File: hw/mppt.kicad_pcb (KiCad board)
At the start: 4 copper layers, 100 x 55 mm, 90 parts, among them J201 1935776, J202 BNC, J301 1935776, J302 1935776, J401 BNC, Q301 SW_L, Q302 SW_H, SW201 SW_Push, U201 MCU_Nucleo_L432KC, U401 OPA990, U402 INA210, U403 OPA990, U404 INA210, U501 LMG1210RVRT

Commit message: fixes for v0.1.1rc
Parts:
- removed C3042, C3052: 15uF, Capacitor_THT:C_Radial_D8.0mm_H11.5mm_P3.50mm
- C303: value 1uF -> 2.2uF
- moved REF** 1.25 mm to (128.2, 97.0)
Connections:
- U201 pad 5: /controller/Error -> unconnected-(U201-D2-Pad5)
- U201 pad 6: unconnected-(U201-D3-Pad6) -> /controller/Error
- U401 pad 1: /controller/ARR_V -> Net-(U401-IN+)
- U401 pad 3: Net-(U401-IN+) -> /controller/ARR_V
- U403 pad 1: /controller/BATT_V -> Net-(U403-IN+)
- U403 pad 3: Net-(U403-IN+) -> /controller/BATT_V
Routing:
- net /controller/Error: track 37.9 -> 40.4 mm
- net Net-(U403-IN+): track 6.05 -> 5.55 mm, vias 3 -> 2
- net GND: vias 524 -> 522
- net /V_ARR+: vias 168 -> 154
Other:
- board text added: "Sunscatter MPPT LHR Solar 2023 Jacob Pustilnik Matthew Yu v0.1.1"
- board text removed: "Jacob Pustilnik Matthew Yu ECE394J Sp2023"

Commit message: v0.2.0
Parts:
- removed D301: Schottky, TestPoint:TestPoint_2Pads_Pitch2.54mm_Drill0.8mm
- removed D302: D_TVS, Diode_SMD:D_SMC
- removed G***: LOGO, graphics:Texas Engineering
- removed HS301: Heatsink_Pad, mppt:WayinTop_HS
- removed J202, J401: BNC, mppt:CONBNC002
- removed R301: R, TestPoint:TestPoint_2Pads_Pitch2.54mm_Drill0.8mm
- removed the REF** at (128.2, 97.0)
- removed SW201: SW_Push, mppt:TS046643BK100SMT
- removed TJ104, TJ105: Thermal Jumper, Resistor_SMD:R_0805_2012Metric
- removed TJ106, TJ107: Thermal Jumper, mppt:1225_SMD
- removed TP205: GND MCU TP, TestPoint:TestPoint_Keystone_5000-5004_Miniature
- removed TP302: TestPoint_2Pole, mppt:SignalTP
- removed U401, U403: OPA990, mppt:SOT65P210X110-5N
- removed U402, U404: INA210, Package_TO_SOT_SMD:SOT-363_SC-70-6_Handsoldering
- removed U501: LMG1210RVRT, mppt:IC_LMG1210RVRT
- added C601: 10uF, Capacitor_SMD:C_0402_1005Metric, B.Cu at (125.5, 54.8)
- added C602: 100nF, Capacitor_SMD:C_0402_1005Metric, B.Cu at (126.9, 54.8)
- added C603: 100nF, Capacitor_SMD:C_0402_1005Metric, B.Cu at (125.5, 52.5)
- added C604: 10nF, Capacitor_SMD:C_0402_1005Metric, B.Cu at (126.9, 52.5)
- added C605: 220nF, Capacitor_SMD:C_0402_1005Metric, B.Cu at (117.5, 54.9)
- added C606: 10uF, Capacitor_SMD:C_0402_1005Metric, B.Cu at (113.6, 55.0)
- added C607: 10nF, Capacitor_SMD:C_0402_1005Metric, B.Cu at (116.2, 52.0)
- added C608: 100nF, Capacitor_SMD:C_0402_1005Metric, B.Cu at (114.8, 52.0)
- added D204: BLUE, LED_SMD:LED_0603_1608Metric, F.Cu at (184.0, 57.2)
- added D205: BLUE, LED_SMD:LED_0603_1608Metric, F.Cu at (184.0, 59.8)
- added D601: CDSOT23-T24CAN, footprints:bourns_CDSOT23_T24CAN, B.Cu at (122.6, 48.7)
- added F301: Fuse_Small, footprints:littelfuse_05200101Z, F.Cu at (90.3, 72.5)
- added F302: Fuse_Small, footprints:littelfuse_05200101Z, F.Cu at (175.6, 72.4)
- added IC401: INA210CQDCKRQ1, footprints:ti_INA210CQDCKRQ1, B.Cu at (102.5, 66.2)
- added IC402: OPA990IDCKR, footprints:ti_OPA990IDCKR, B.Cu at (118.7, 66.0)
- added IC403: OPA990IDCKR, footprints:ti_OPA990IDCKR, B.Cu at (178.3, 66.0)
- added IC404: INA210CQDCKRQ1, footprints:ti_INA210CQDCKRQ1, B.Cu at (187.7, 66.1)
- added IC501: LMG1210RVRT, footprints:ti_LMG1210RVRT, F.Cu at (166.6, 75.2)
- added IC601: ADM3055EBRIZ, footprints:analog_ADM3055EBRIZ, F.Cu at (124.1, 51.0)
- added J601: 43650-0427, footprints:molex_microfit_43650_0427, F.Cu at (97.7, 55.5)
- added J602: 43650-0427, footprints:molex_microfit_43650_0427, F.Cu at (108.3, 55.5)
- added JP601: Termination Resistors, Connector_PinHeader_2.54mm:PinHeader_1x02_P2.54mm_Vertical, F.Cu at (115.5, 43.7)
- added L601: 1.8k, Inductor_SMD:L_0402_1005Metric, B.Cu at (115.5, 55.6)
- added L602: 1.8k, Inductor_SMD:L_0402_1005Metric, B.Cu at (115.5, 54.2)
- added R203: 100, Resistor_SMD:R_0402_1005Metric, B.Cu at (168.6, 46.4)
- added R204: 100, Resistor_SMD:R_0402_1005Metric, B.Cu at (158.4, 46.4)
- added R205: 100, Resistor_SMD:R_0402_1005Metric, B.Cu at (138.1, 46.4)
- added R601: 0, Resistor_SMD:R_0402_1005Metric, B.Cu at (117.5, 46.0)
- added R602: 60.4, Resistor_SMD:R_0402_1005Metric, B.Cu at (115.5, 49.4)
- added R603: 60.4, Resistor_SMD:R_0402_1005Metric, B.Cu at (113.8, 49.5)
- added REF**: ESD-Logo_6.6x6mm_SilkScreen, Symbol:ESD-Logo_6.6x6mm_SilkScreen, B.Cu at (131.1, 91.0)
- added S201: TS-1187A-B-A-B, footprints:xkb_TS_1187A_B_A_B, F.Cu at (184.0, 45.0)
- added TP411: BATTV_TP, TestPoint:TestPoint_Pad_1.0x1.0mm, F.Cu at (161.9, 63.9)
- added TP412: BATTI_TP, TestPoint:TestPoint_Pad_1.0x1.0mm, F.Cu at (169.0, 63.9)
- added TP504: PWMEN_TP, TestPoint:TestPoint_Pad_1.0x1.0mm, B.Cu at (166.3, 70.7)
- added TP505: PWM_TP, TestPoint:TestPoint_Pad_1.0x1.0mm, B.Cu at (164.3, 70.7)
- added TP601: CAN RX TP, TestPoint:TestPoint_Pad_1.0x1.0mm, B.Cu at (128.9, 51.7)
- added TP602: CAN TX TP, TestPoint:TestPoint_Pad_1.0x1.0mm, B.Cu at (128.9, 49.1)
- added TP603: CAN L TP, TestPoint:TestPoint_Pad_1.0x1.0mm, B.Cu at (119.3, 47.7)
- added TP604: CAN H TP, TestPoint:TestPoint_Pad_1.0x1.0mm, B.Cu at (119.3, 49.3)
- added kibuzzard-64BB9525: G***, kibuzzard-64BB9525, F.Cu at (189.4, 52.3)
- added kibuzzard-64BB9530: G***, kibuzzard-64BB9530, F.Cu at (189.4, 49.8)
- added kibuzzard-64BB9539: G***, kibuzzard-64BB9539, F.Cu at (189.4, 54.8)
- added kibuzzard-64BB9548: G***, kibuzzard-64BB9548, F.Cu at (189.4, 59.9)
- added kibuzzard-64BB954F: G***, kibuzzard-64BB954F, F.Cu at (189.4, 57.2)
- added kibuzzard-64BB9585: G***, kibuzzard-64BB9585, F.Cu at (189.4, 45.0)
- added kibuzzard-64BB95E9: G***, kibuzzard-64BB95E9, F.Cu at (204.2, 57.0)
- added kibuzzard-64BB964A: G***, kibuzzard-64BB964A, F.Cu at (201.1, 53.0)
- added kibuzzard-64BB966B: G***, kibuzzard-64BB966B, F.Cu at (201.1, 56.0)
- added kibuzzard-64BB968B: G***, kibuzzard-64BB968B, F.Cu at (175.3, 51.0)
- added kibuzzard-64BB971E: G***, kibuzzard-64BB971E, F.Cu at (90.8, 58.8)
- added kibuzzard-64BB973A: G***, kibuzzard-64BB973A, F.Cu at (103.2, 46.5)
- added kibuzzard-64BB974F: G***, kibuzzard-64BB974F, F.Cu at (103.2, 49.5)
- added kibuzzard-64BB975A: G***, kibuzzard-64BB975A, F.Cu at (103.2, 55.5)
- added kibuzzard-64BB9776: G***, kibuzzard-64BB9776, F.Cu at (103.2, 52.5)
- added kibuzzard-64BB97BE: G***, kibuzzard-64BB97BE, F.Cu at (89.2, 90.8)
- added kibuzzard-64BB97CA: G***, kibuzzard-64BB97CA, F.Cu at (199.6, 90.8)
- added kibuzzard-64BB97F0: G***, kibuzzard-64BB97F0, B.Cu at (106.0, 98.3)
- added kibuzzard-64BB97F0: G***, kibuzzard-64BB97F0, B.Cu at (191.3, 98.2)
- added kibuzzard-64BB97FE: G***, kibuzzard-64BB97FE, B.Cu at (183.9, 98.1)
- added kibuzzard-64BB97FE: G***, kibuzzard-64BB97FE, B.Cu at (98.7, 98.3)
- added kibuzzard-64BB9873: G***, kibuzzard-64BB9873, F.Cu at (88.7, 87.8)
- added kibuzzard-64BB9873: G***, kibuzzard-64BB9873, F.Cu at (201.3, 87.8)
- added kibuzzard-64BB98F2: G***, kibuzzard-64BB98F2, F.Cu at (88.3, 81.6)
- added kibuzzard-64BB98F8: G***, kibuzzard-64BB98F8, F.Cu at (88.3, 84.7)
- added kibuzzard-64BB9946: G***, kibuzzard-64BB9946, F.Cu at (201.9, 84.7)
- added kibuzzard-64BB994C: G***, kibuzzard-64BB994C, F.Cu at (202.0, 81.5)
- added kibuzzard-64BBA694: G***, kibuzzard-64BBA694, F.Cu at (129.8, 63.8)
- added kibuzzard-64BBA6A3: G***, kibuzzard-64BBA6A3, F.Cu at (136.4, 63.8)
- added kibuzzard-64BBA6B0: G***, kibuzzard-64BBA6B0, F.Cu at (162.1, 66.2)
- added kibuzzard-64BBA6B0: G***, kibuzzard-64BBA6B0, F.Cu at (132.9, 66.0)
- added kibuzzard-64BBA752: G***, kibuzzard-64BBA752, F.Cu at (158.4, 63.9)
- added kibuzzard-64BBA758: G***, kibuzzard-64BBA758, F.Cu at (165.6, 63.9)
- added kibuzzard-64BBA88C: G***, kibuzzard-64BBA88C, B.Cu at (160.9, 54.1)
- added kibuzzard-64BBA896: G***, kibuzzard-64BBA896, B.Cu at (165.7, 54.0)
- added kibuzzard-64BBA8A0: G***, kibuzzard-64BBA8A0, B.Cu at (168.9, 54.0)
- added kibuzzard-64BBA8B2: G***, kibuzzard-64BBA8B2, B.Cu at (138.0, 56.0)
- added kibuzzard-64BBA8C3: G***, kibuzzard-64BBA8C3, B.Cu at (163.9, 68.8)
- added kibuzzard-64BBA8E6: G***, kibuzzard-64BBA8E6, B.Cu at (166.3, 68.8)
- added kibuzzard-64BBA9B6: G***, kibuzzard-64BBA9B6, F.Cu at (142.2, 67.5)
- added kibuzzard-64BBA9C0: G***, kibuzzard-64BBA9C0, F.Cu at (147.3, 67.4)
- added kibuzzard-64BBA9D4: G***, kibuzzard-64BBA9D4, F.Cu at (152.3, 67.4)
- added kibuzzard-64BBAA49: G***, kibuzzard-64BBAA49, F.Cu at (155.2, 78.3)
- added kibuzzard-64BBAA54: G***, kibuzzard-64BBAA54, F.Cu at (155.2, 73.2)
- added kibuzzard-64BC07CB: G***, kibuzzard-64BC07CB, B.Cu at (131.0, 49.1)
- added kibuzzard-64BC07D4: G***, kibuzzard-64BC07D4, B.Cu at (131.0, 51.7)
- added kibuzzard-64BC07E0: G***, kibuzzard-64BC07E0, B.Cu at (117.5, 47.7)
- added kibuzzard-64BC07EC: G***, kibuzzard-64BC07EC, B.Cu at (117.5, 49.3)
- C301: value 15uF -> 2.2uF; footprint Capacitor_THT:C_Radial_D8.0mm_H11.5mm_P3.50mm -> Capacitor_SMD:C_2220_5650Metric; moved to B.Cu
- C302: value CP -> 15uF; footprint TestPoint:TestPoint_2Pads_Pitch2.54mm_Drill0.8mm -> Capacitor_THT:C_Radial_D8.0mm_H11.5mm_P3.50mm
- C503: value 1uF -> 10uF; footprint Capacitor_SMD:C_0402_1005Metric -> Capacitor_SMD:C_0603_1608Metric
- C505: value 10uF -> 1uF; footprint Capacitor_SMD:C_0603_1608Metric -> Capacitor_SMD:C_0402_1005Metric
- D201: value RED -> YELLOW; footprint LED_SMD:LED_0402_1005Metric -> LED_SMD:LED_0603_1608Metric
- D202: value YELLOW -> GREEN; footprint LED_SMD:LED_0402_1005Metric -> LED_SMD:LED_0603_1608Metric
- D203: value BLUE -> GREEN; footprint LED_SMD:LED_0402_1005Metric -> LED_SMD:LED_0603_1608Metric
- D402, D403: value 3.3V Zener -> 3V3
- D501: value 0.62V Schottky -> 0.62V; footprint mppt:SODFL5226X110N -> footprints:stm_STPS1170AF
- H101, H102, H103, H104: footprint MountingHole:MountingHole_3.5mm -> MountingHole:MountingHole_3.2mm_M3
- J201: value 1935776 -> 43650-0227; footprint mppt:1935776 -> footprints:molex_microfit_43650_0227
- J301, J302: value 1935776 -> XT60PW-M; footprint mppt:1935776 -> Connector_AMASS:AMASS_XT60PW-M_1x02_P7.20mm_Horizontal
- L301: footprint mppt:B65878E1012D001 -> footprints:tdk_B65878E1012D001
- Q301, Q302: footprint mppt:EPC2307 -> footprints:epc_EPC2307
- R502: value 20k -> 1.8
- R503: value 1.8 -> 20k
- TJ101, TJ102, TJ103: footprint mppt:1225_SMD -> footprints:vishay_THJP1225ABT1; moved to B.Cu
- TP201: value 5V TP -> 3V3 TP; footprint TestPoint:TestPoint_Keystone_5000-5004_Miniature -> TestPoint:TestPoint_Pad_1.0x1.0mm
- TP202: value 3.3V TP -> 5V TP; footprint TestPoint:TestPoint_Keystone_5000-5004_Miniature -> TestPoint:TestPoint_Pad_1.0x1.0mm; moved to B.Cu
- TP203: value 12V TP -> GND TP; footprint TestPoint:TestPoint_Keystone_5000-5004_Miniature -> TestPoint:TestPoint_Pad_1.0x1.0mm
- TP204: value TestPoint_2Pole -> 12V TP; footprint mppt:SignalTP -> TestPoint:TestPoint_Pad_1.0x1.0mm; moved to B.Cu
- TP301: value TestPoint_2Pole -> VSW_TP; footprint mppt:SignalTP -> TestPoint:TestPoint_2Pads_Pitch5.08mm_Drill1.3mm
- TP401: value TestPoint_2Pole -> +ARR_TP; footprint mppt:SignalTP -> TestPoint:TestPoint_Pad_1.0x1.0mm
- TP402: value GND -> GND_TP; footprint TestPoint:TestPoint_Keystone_5000-5004_Miniature -> TestPoint:TestPoint_Pad_1.0x1.0mm
- TP403: value -ARR -> GND_TP; footprint TestPoint:TestPoint_Keystone_5000-5004_Miniature -> TestPoint:TestPoint_Pad_1.0x1.0mm
- TP404: value Array Current -> -ARR_TP; footprint TestPoint:TestPoint_Keystone_5000-5004_Miniature -> TestPoint:TestPoint_Pad_1.0x1.0mm
- TP405: value Array Voltage -> ARRI_TP; footprint TestPoint:TestPoint_Keystone_5000-5004_Miniature -> TestPoint:TestPoint_Pad_1.0x1.0mm
- TP406: value -BATT -> ARRV_TP; footprint TestPoint:TestPoint_Keystone_5000-5004_Miniature -> TestPoint:TestPoint_Pad_1.0x1.0mm
- TP407: value GND -> +BATT_TP; footprint TestPoint:TestPoint_Keystone_5000-5004_Miniature -> TestPoint:TestPoint_Pad_1.0x1.0mm
- TP408: value Battery Current -> GND_TP; footprint TestPoint:TestPoint_Keystone_5000-5004_Miniature -> TestPoint:TestPoint_Pad_1.0x1.0mm
- TP409: value Battery Voltage -> -BATT_TP; footprint TestPoint:TestPoint_Keystone_5000-5004_Miniature -> TestPoint:TestPoint_Pad_1.0x1.0mm
- TP410: value TestPoint_2Pole -> GND_TP; footprint mppt:SignalTP -> TestPoint:TestPoint_Pad_1.0x1.0mm
- TP501: value TestPoint_2Pole -> SW1_TP; footprint mppt:SignalTP -> TestPoint:TestPoint_Keystone_5005-5009_Compact
- TP502: value TestPoint_2Pole -> GND_TP; footprint mppt:SignalTP -> TestPoint:TestPoint_Keystone_5005-5009_Compact
- TP503: value TestPoint_2Pole -> SW2_TP; footprint mppt:SignalTP -> TestPoint:TestPoint_Keystone_5005-5009_Compact
- U201: value MCU_Nucleo_L432KC -> NUCLEO-L432KC; footprint mppt:MODULE_NUCLEO-L432KC -> footprints:stm_nucleo_L432KC
- moved H101 111.3 mm to (201.5, 96.5)
- moved H102 101.6 mm to (88.5, 96.5)
- moved J201 97.1 mm to (197.6, 53.0), turned to 90 degrees
- moved C201 91.7 mm to (195.2, 54.5), turned to -90 degrees
- moved H104 74.4 mm to (201.5, 43.4)
- moved H103 72.9 mm to (88.5, 43.5)
- moved TP406 71.0 mm to (133.2, 63.9)
- moved TP403 57.9 mm to (130.5, 66.1)
- moved TP204 52.7 mm to (168.6, 56.0), turned to -90 degrees
- moved TP202 51.7 mm to (160.9, 56.0), turned to -90 degrees
- moved TP203 51.3 mm to (166.0, 56.0), turned to -90 degrees
- moved C302 39.8 mm to (114.5, 93.8), turned to 0 degrees
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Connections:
- C302 pad 1: /converter/Vsnub -> /V_ARR+
- C401 pad 2: +12V -> +5V
- C402 pad 2: +12V -> +5V
- C403 pad 2: +12V -> +5V
- C404 pad 2: +12V -> +5V
- C501 pad 1: +12V -> +5V
- C502 pad 1: +12V -> +5V
- C503 pad 1: /V_SW -> +12V
- C503 pad 2: /gate_driver/HB -> GND
- C504 pad 1: +5V -> +12V
- C505 pad 1: +5V -> Net-(D501-K)
- C505 pad 2: GND -> /V_SW
- D203 pad 2: /controller/Heartbeat -> Net-(D203-A)
- D403 pad 1: /controller/BATT_I -> /controller/BATT_V
- D404 pad 1: /controller/BATT_V -> /controller/BATT_I
- D501 pad 1: /gate_driver/HB -> Net-(D501-K)
- D501 pad 2: /gate_driver/BST -> Net-(D501-A)
- J301 pad 1: /V_ARR+ -> Net-(F301-Pad1)
- J302 pad 1: /V_BATT+ -> Net-(F302-Pad2)
- R501 pad 1: /gate_driver/DLH -> Net-(IC501-DHL)
- R502 pad 1: /gate_driver/DHL -> /converter/G1
- R502 pad 2: GND -> Net-(IC501-LO)
- R503 pad 1: /gate_driver/LO -> GND
- R503 pad 2: /converter/G1 -> Net-(IC501-DLH)
- R504 pad 1: /gate_driver/HO -> /converter/G2
- R504 pad 2: /converter/G2 -> Net-(IC501-HO)
- TJ102 pad 1: /V_SW -> GND
- TJ102 pad 2: /V_ARR+ -> /V_BATT+
- TJ103 pad 1: /V_SW -> GND
- TJ103 pad 2: +12V -> GND
- TP201 pad 1: +5V -> +3V3
- TP202 pad 1: +3.3V -> +5V
- TP203 pad 1: +12V -> GND
- TP204 pad 1: /controller/PWM_CTRL -> +12V
- TP301 pad 1: /converter/Vsnub -> /V_SW
- TP403 pad 1: /converter/V_ARR- -> GND
- TP404 pad 1: /controller/ARR_I -> /converter/V_ARR-
- TP405 pad 1: /controller/ARR_V -> /controller/ARR_I
- TP406 pad 1: /converter/V_BATT- -> /controller/ARR_V
- TP407 pad 1: GND -> /V_BATT+
- TP408 pad 1: /controller/BATT_I -> GND
- TP409 pad 1: /controller/BATT_V -> /converter/V_BATT-
- TP410 pad 1: /V_BATT+ -> GND
- TP501 pad 1: /controller/PWM -> /converter/G1
- TP502 pad 1: /converter/G1 -> GND
- U201 pad 13: unconnected-(U201-D10-Pad13) -> /CAN_RX
- U201 pad 17: +3.3V -> +3V3
- U201 pad 19: /controller/PWM_CTRL -> /controller/ARR_I
- U201 pad 20: /controller/PWM -> /controller/ARR_V
- U201 pad 21: /controller/PWM_EN -> unconnected-(U201-A2-Pad21)
- U201 pad 22: /controller/ARR_V -> unconnected-(U201-A3-Pad22)
- U201 pad 23: /controller/ARR_I -> /controller/PWM_EN
- U201 pad 24: /controller/BATT_I -> /controller/PWM
- U201 pad 26: unconnected-(U201-A7-Pad26) -> /controller/BATT_I
- U201 pad 5: unconnected-(U201-D2-Pad5) -> /CAN_TX
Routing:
- net Net-(D205-A): track 0.00 -> 52.3 mm, vias 0 -> 3
- net +12V: track 18.1 -> 59.8 mm, vias 6 -> 1
- net Net-(D601-K3): track 0.00 -> 39.8 mm, vias 0 -> 3
- net /controller/Error: track 40.4 -> 2.41 mm, vias 1 -> 0
- net /CAN_TX: track 0.00 -> 35.7 mm, vias 0 -> 3
- net /controller/BATT_V: track 62.3 -> 28.0 mm, vias 2 -> 1
- net GND: track 44.5 -> 76.9 mm, vias 522 -> 111
- net Net-(D201-A): track 0.00 -> 31.0 mm, vias 1 -> 3
- net Net-(D204-A): track 0.00 -> 29.1 mm, vias 0 -> 1
- net /comm_can/CAN_L: track 0.00 -> 26.9 mm, vias 0 -> 2
- net /controller/Tracking: track 29.1 -> 2.42 mm, vias 1 -> 0
- net Net-(IC601-VISOIN): track 0.00 -> 26.0 mm, vias 0 -> 2
- net /comm_can/CAN_H: track 0.00 -> 25.4 mm, vias 0 -> 2
- net /controller/Heartbeat: track 27.3 -> 2.41 mm, vias 1 -> 0
- net /V_ARR+: track 3.54 -> 26.8 mm, vias 154 -> 25
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- added copper zone on F.Cu, net +5V
- added copper zone on In1.Cu, net +5V
- added copper zone on F.Cu, net Net-(F301-Pad1)
- added copper zone on In1.Cu, net Net-(F301-Pad1)
- added copper zone on F.Cu, net Net-(F302-Pad2)
- added copper zone on In1.Cu, net Net-(F302-Pad2)
- removed copper zone on F.Cu, net +12V
- removed copper zone on B.Cu, net /V_SW
- removed copper zone on In2.Cu, net /V_SW
- removed copper zone on In1.Cu, net GND
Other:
- board size 100 x 55 mm -> 120.1 x 60 mm
- board text added: "LHR Solar Sunscatter Gen 2 v0.2.0 Summer 2023 Matthew Yu"
- board text added: "LHRS Sunscatter Gen 2 v0.2.0"
- board text added: "Trace should not modify fill. Used to remove DRC."
- board text removed: "+"
- board text removed: "+12V"
- board text removed: "."
- board text removed: "ARR+"
- board text removed: "ARR-"
- board text removed: "BATT+"
- board text removed: "BATT-"
- board text removed: "GND"
- board text removed: "Sunscatter MPPT LHR Solar 2023 Jacob Pustilnik Matthew Yu v0.1.1"
- board text removed: "USB ^^^"

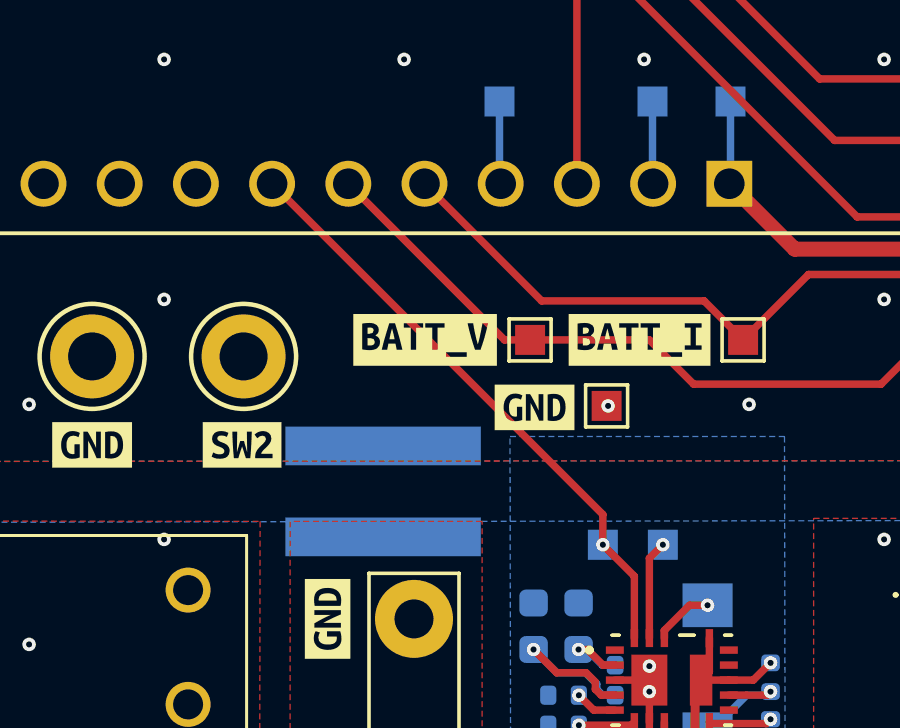
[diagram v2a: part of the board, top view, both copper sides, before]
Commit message: bugfix for wrong adc pin for batt current measurements
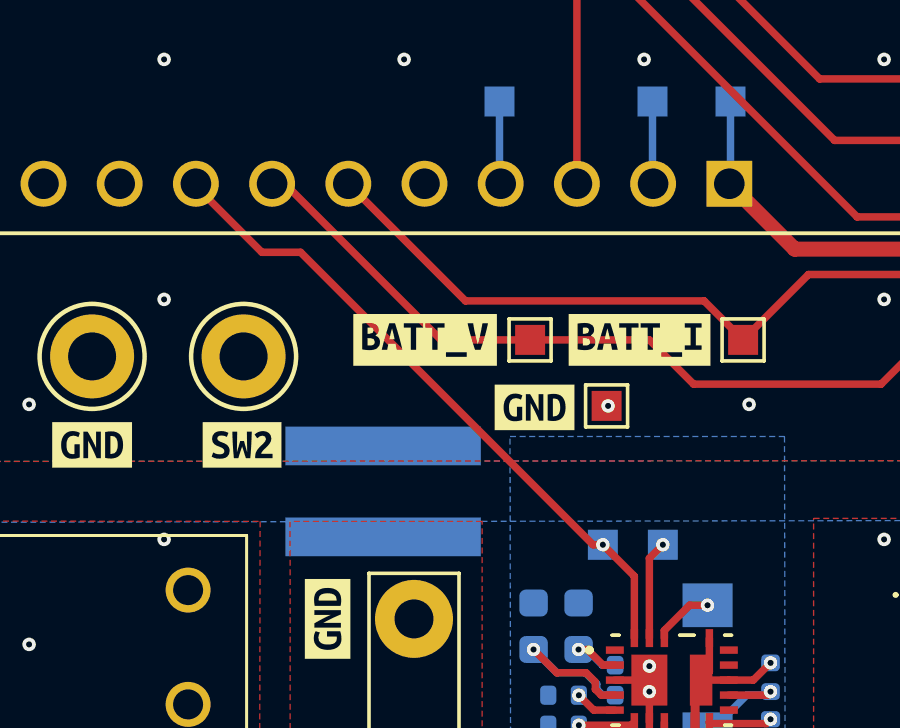
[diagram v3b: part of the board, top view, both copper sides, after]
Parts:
- H101: value Top Left Mounting Hole -> M3 Mounting Hole
- H102: value Top Right Mounting Hole -> M3 Mounting Hole
- H103: value Bottom Left Mounting Hole -> M3 Mounting Hole
- H104: value Bottom Right Mounting Hole -> M3 Mounting Hole
- Q301: value SW_L -> EPC2307
- Q302: value SW_H -> EPC2307
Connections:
- U201 pad 22: unconnected-(U201-A3-Pad22) -> /controller/PWM_EN
- U201 pad 23: /controller/PWM_EN -> /controller/PWM
- U201 pad 24: /controller/PWM -> /controller/BATT_V
- U201 pad 25: /controller/BATT_V -> /controller/BATT_I
- U201 pad 26: /controller/BATT_I -> unconnected-(U201-A7-Pad26)
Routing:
- net /controller/PWM_EN: track 23.8 -> 26.4 mm
- net /controller/BATT_I: track 33.9 -> 36.4 mm
- net /controller/BATT_V: track 28.0 -> 30.5 mm
- net /controller/PWM: track 20.1 -> 22.1 mm

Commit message: fix for swapped xt60 connectors
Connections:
- J301 pad 1: Net-(F301-Pad1) -> /converter/V_ARR-
- J301 pad 2: /converter/V_ARR- -> Net-(F301-Pad1)
- J302 pad 1: Net-(F302-Pad2) -> /converter/V_BATT-
- J302 pad 2: /converter/V_BATT- -> Net-(F302-Pad2)
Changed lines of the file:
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@@
         (effects (font (size 0.8 0.8) (thickness 0.15)))
     )
-    (fp_text user "+" (at -3.95 2.05) (layer "F.SilkS")
+    (fp_text user "+" (at 11.14 2.04) (layer "F.SilkS")
         (effects (font (size 0.8 0.8) (thickness 0.15)))
     )
-    (fp_text user "-" (at 11 2.05) (layer "F.SilkS")
+    (fp_text user "-" (at -3.49 2.01) (layer "F.SilkS")
         (effects (font (size 0.8 0.8) (thickness 0.15)))
     )
@@
     (pad "" thru_hole rect (at 10.35 -6 180) (size 0.9 2) (drill oval 0.6 1.7) (layers "*.Cu" "*.Mask"))
     (pad "1" thru_hole roundrect (at 0 0 180) (size 4.1 4.1) (drill 2.7) (layers "*.Cu" "*.Mask") (roundrect_rratio 0.25)
-      (net 63 "Net-(F301-Pad1)") (pinfunction "1") (pintype "passive"))
+      (net 5 "/converter/V_ARR-") (pinfunction "1") (pintype "passive"))
     (pad "2" thru_hole circle (at 7.2 0 180) (size 4.1 4.1) (drill 2.7) (layers "*.Cu" "*.Mask")
-      (net 5 "/converter/V_ARR-") (pinfunction "2") (pintype "passive"))
+      (net 63 "Net-(F301-Pad1)") (pinfunction "2") (pintype "passive"))
     (model "${KICAD6_3DMODEL_DIR}/Connector_AMASS.3dshapes/AMASS_XT60PW-M_1x02_P7.20mm_Horizontal.wrl"
       (offset (xyz 0 0 0))
@@
     (property "ki_keywords" "transistor NMOS N-MOS N-MOSFET")
     (attr smd)
-    (fp_text reference "Q302" (at 0 -3.2 unlocked) (layer "F.SilkS")
+    (fp_text reference "Q302" (at 0 -3.2 unlocked) (layer "F.SilkS") hide
         (effects (font (size 1 1) (thickness 0.15)))
     )
@@
     (property "ki_keywords" "transistor NMOS N-MOS N-MOSFET")
     (attr smd)
-    (fp_text reference "Q301" (at 0 -3.2 unlocked) (layer "F.SilkS")
+    (fp_text reference "Q301" (at 0 -3.2 unlocked) (layer "F.SilkS") hide
         (effects (font (size 1 1) (thickness 0.15)))
     )
@@
         (effects (font (size 0.8 0.8) (thickness 0.15)))
     )
-    (fp_text user "-" (at 11.05 2.05) (layer "F.SilkS")
+    (fp_text user "+" (at 10.87 1.91) (layer "F.SilkS")
         (effects (font (size 0.8 0.8) (thickness 0.15)))
     )
-    (fp_text user "+" (at -4.05 1.85) (layer "F.SilkS")
+    (fp_text user "-" (at -3.51 1.83) (layer "F.SilkS")
         (effects (font (size 0.8 0.8) (thickness 0.15)))
     )
@@
     (pad "" thru_hole rect (at 10.35 -6 180) (size 0.9 2) (drill oval 0.6 1.7) (layers "*.Cu" "*.Mask"))
     (pad "1" thru_hole roundrect (at 0 0 180) (size 4.1 4.1) (drill 2.7) (layers "*.Cu" "*.Mask") (roundrect_rratio 0.25)
-      (net 64 "Net-(F302-Pad2)") (pinfunction "1") (pintype "passive"))
+      (net 6 "/converter/V_BATT-") (pinfunction "1") (pintype "passive"))
     (pad "2" thru_hole circle (at 7.2 0 180) (size 4.1 4.1) (drill 2.7) (layers "*.Cu" "*.Mask")
-      (net 6 "/converter/V_BATT-") (pinfunction "2") (pintype "passive"))
-    (model "${KICAD6_3DMODEL_DIR}/Connector_AMASS.3dshapes/AMASS_XT60PW-M_1x02_P7.20mm_Horizontal.wrl"
-      (offset (xyz 0 0 0))
-      (scale (xyz 1 1 1))
-      (rotate (xyz 0 0 0))
-    )
+      (net 64 "Net-(F302-Pad2)") (pinfunction "2") (pintype "passive"))
     (model "${KIPRJMOD}/models/amass_XT60PW_M.STEP"
       (offset (xyz 3.5 6 0))
@@
   )
   (dimension (type aligned) (layer "Dwgs.User")
-    (pts (xy 88.5 40.05) (xy 88.5 65.05))
+    (pts (xy 88.5 40) (xy 88.5 68))
     (height 8.5)
-    (gr_text "25.0000 mm" (at 78.85 52.55 90) (layer "Dwgs.User")
+    (gr_text "28.0000 mm" (at 78.85 54 90) (layer "Dwgs.User")
       (effects (font (size 1 1) (thickness 0.15)))
     )

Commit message: HW sch changes, further layout progression
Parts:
- removed C404, C608: 100nF, Capacitor_SMD:C_0402_1005Metric
- removed C606: 10uF, Capacitor_SMD:C_0402_1005Metric
- removed C607: 10nF, Capacitor_SMD:C_0402_1005Metric
- removed F301, F302: Fuse_Small, footprints:littelfuse_05200101Z
- removed IC401, IC404: INA210CQDCKRQ1, footprints:ti_INA210CQDCKRQ1
- removed IC402, IC403: OPA990IDCKR, footprints:ti_OPA990IDCKR
- removed IC501: LMG1210RVRT, footprints:ti_LMG1210RVRT
- removed IC601: ADM3055EBRIZ, footprints:analog_ADM3055EBRIZ
- removed J302: XT60PW-M, Connector_AMASS:AMASS_XT60PW-M_1x02_P7.20mm_Horizontal
- removed JP601: Termination Resistors, Connector_PinHeader_2.54mm:PinHeader_1x02_P2.54mm_Vertical
- removed L602: 1.8k, Inductor_SMD:L_0402_1005Metric
- removed Q302: EPC2307, footprints:epc_EPC2307
- removed R601: 0, Resistor_SMD:R_0402_1005Metric
- removed R602, R603: 60.4, Resistor_SMD:R_0402_1005Metric
- removed REF**: ESD-Logo_6.6x6mm_SilkScreen, Symbol:ESD-Logo_6.6x6mm_SilkScreen
- removed REF**: KiCad-Logo2_5mm_SilkScreen, Symbol:KiCad-Logo2_5mm_SilkScreen
- removed S201: TS-1187A-B-A-B, footprints:xkb_TS_1187A_B_A_B
- removed TJ101, TJ102, TJ103: Thermal Jumper, footprints:vishay_THJP1225ABT1
- removed TP201: 3V3 TP, TestPoint:TestPoint_Pad_1.0x1.0mm
- removed TP202: 5V TP, TestPoint:TestPoint_Pad_1.0x1.0mm
- removed TP203: GND TP, TestPoint:TestPoint_Pad_1.0x1.0mm
- removed TP204: 12V TP, TestPoint:TestPoint_Pad_1.0x1.0mm
- removed TP409: -BATT_TP, TestPoint:TestPoint_Pad_1.0x1.0mm
- removed TP410: GND_TP, TestPoint:TestPoint_Pad_1.0x1.0mm
- removed TP411: BATTV_TP, TestPoint:TestPoint_Pad_1.0x1.0mm
- removed TP412: BATTI_TP, TestPoint:TestPoint_Pad_1.0x1.0mm
- removed TP601: CAN RX TP, TestPoint:TestPoint_Pad_1.0x1.0mm
- removed TP602: CAN TX TP, TestPoint:TestPoint_Pad_1.0x1.0mm
- removed TP603: CAN L TP, TestPoint:TestPoint_Pad_1.0x1.0mm
- removed TP604: CAN H TP, TestPoint:TestPoint_Pad_1.0x1.0mm
- removed kibuzzard-64BB9525: G***, kibuzzard-64BB9525
- removed kibuzzard-64BB9530: G***, kibuzzard-64BB9530
- removed kibuzzard-64BB9539: G***, kibuzzard-64BB9539
- removed kibuzzard-64BB9548: G***, kibuzzard-64BB9548
- removed kibuzzard-64BB954F: G***, kibuzzard-64BB954F
- removed kibuzzard-64BB9585: G***, kibuzzard-64BB9585
- removed kibuzzard-64BB95E9: G***, kibuzzard-64BB95E9
- removed kibuzzard-64BB964A: G***, kibuzzard-64BB964A
- removed kibuzzard-64BB966B: G***, kibuzzard-64BB966B
- removed kibuzzard-64BB968B: G***, kibuzzard-64BB968B
- removed kibuzzard-64BB971E: G***, kibuzzard-64BB971E
- removed kibuzzard-64BB973A: G***, kibuzzard-64BB973A
- removed kibuzzard-64BB974F: G***, kibuzzard-64BB974F
- removed kibuzzard-64BB975A: G***, kibuzzard-64BB975A
- removed kibuzzard-64BB9776: G***, kibuzzard-64BB9776
- removed kibuzzard-64BB97BE: G***, kibuzzard-64BB97BE
- removed kibuzzard-64BB97CA: G***, kibuzzard-64BB97CA
- removed kibuzzard-64BB97F0 (x2): G***, kibuzzard-64BB97F0
- removed kibuzzard-64BB97FE (x2): G***, kibuzzard-64BB97FE
- removed kibuzzard-64BB9873 (x2): G***, kibuzzard-64BB9873
- removed kibuzzard-64BB98F2: G***, kibuzzard-64BB98F2
- removed kibuzzard-64BB98F8: G***, kibuzzard-64BB98F8
- removed kibuzzard-64BB9946: G***, kibuzzard-64BB9946
- removed kibuzzard-64BB994C: G***, kibuzzard-64BB994C
- removed kibuzzard-64BBA694: G***, kibuzzard-64BBA694
- removed kibuzzard-64BBA6A3: G***, kibuzzard-64BBA6A3
- removed kibuzzard-64BBA6B0 (x2): G***, kibuzzard-64BBA6B0
- removed kibuzzard-64BBA752: G***, kibuzzard-64BBA752
- removed kibuzzard-64BBA758: G***, kibuzzard-64BBA758
- removed kibuzzard-64BBA88C: G***, kibuzzard-64BBA88C
- removed kibuzzard-64BBA896: G***, kibuzzard-64BBA896
- removed kibuzzard-64BBA8A0: G***, kibuzzard-64BBA8A0
- removed kibuzzard-64BBA8B2: G***, kibuzzard-64BBA8B2
- removed kibuzzard-64BBA8C3: G***, kibuzzard-64BBA8C3
- removed kibuzzard-64BBA8E6: G***, kibuzzard-64BBA8E6
- removed kibuzzard-64BBA9B6: G***, kibuzzard-64BBA9B6
- removed kibuzzard-64BBA9C0: G***, kibuzzard-64BBA9C0
- removed kibuzzard-64BBA9D4: G***, kibuzzard-64BBA9D4
- removed kibuzzard-64BBAA49: G***, kibuzzard-64BBAA49
- removed kibuzzard-64BBAA54: G***, kibuzzard-64BBAA54
- removed kibuzzard-64BC07CB: G***, kibuzzard-64BC07CB
- removed kibuzzard-64BC07D4: G***, kibuzzard-64BC07D4
- removed kibuzzard-64BC07E0: G***, kibuzzard-64BC07E0
- removed kibuzzard-64BC07EC: G***, kibuzzard-64BC07EC
- added C202: 4.3p, Resistor_SMD:R_0402_1005Metric, B.Cu at (66.4, 39.0)
- added C203: 10u, Resistor_SMD:R_0805_2012Metric, B.Cu at (77.3, 45.8)
- added C204: 100n, Resistor_SMD:R_0402_1005Metric, B.Cu at (70.1, 44.2)
- added C205: 6p, Resistor_SMD:R_0402_1005Metric, B.Cu at (64.8, 47.1)
- added C206: 4.3p, Resistor_SMD:R_0402_1005Metric, B.Cu at (66.4, 42.2)
- added C207: 100n, Resistor_SMD:R_0402_1005Metric, B.Cu at (61.3, 48.9)
- added C208: 100n, Resistor_SMD:R_0402_1005Metric, B.Cu at (71.6, 51.7)
- added C209: 100n, Resistor_SMD:R_0402_1005Metric, B.Cu at (78.1, 51.8)
- added C210: 4.7u, Resistor_SMD:R_0402_1005Metric, B.Cu at (77.0, 51.7)
- added C211: 100n, Resistor_SMD:R_0402_1005Metric, B.Cu at (78.1, 44.2)
- added C212: 100n, Resistor_SMD:R_0402_1005Metric, B.Cu at (71.1, 44.2)
- added C213: 100n, Resistor_SMD:R_0402_1005Metric, B.Cu at (70.6, 50.2)
- added C214: 1u, Resistor_SMD:R_0402_1005Metric, B.Cu at (70.6, 49.2)
- added C306: 1u, Resistor_SMD:R_0402_1005Metric, B.Cu at (256.4, 24.7)
- added C307: 100n, Resistor_SMD:R_0402_1005Metric, B.Cu at (227.8, 28.0)
- added C308: 1u, Resistor_SMD:R_0402_1005Metric, B.Cu at (255.3, 38.3)
- added C309: 22u, Resistor_SMD:R_0805_2012Metric, B.Cu at (227.7, 31.7)
- added C310: 22u, Resistor_SMD:R_0805_2012Metric, B.Cu at (225.7, 31.7)
- added C311: 22u, Resistor_SMD:R_0805_2012Metric, B.Cu at (259.2, 39.7)
- added C312: 1u, Resistor_SMD:R_0402_1005Metric, B.Cu at (254.2, 31.2)
- added C313: 1u, Resistor_SMD:R_0402_1005Metric, B.Cu at (256.4, 31.2)
- added C314: 4.7u, Resistor_SMD:R_0402_1005Metric, B.Cu at (260.1, 48.2)
- added C506: 10n, Resistor_SMD:R_0402_1005Metric, B.Cu at (36.7, 151.3)
- added C507: 10n, Resistor_SMD:R_0402_1005Metric, F.Cu at (123.8, 149.6)
- added C508: 100n, Resistor_SMD:R_0402_1005Metric, B.Cu at (35.3, 150.0)
- added C509: 100n, Resistor_SMD:R_0402_1005Metric, B.Cu at (42.7, 150.0)
- added C510: 100n, Resistor_SMD:R_0402_1005Metric, F.Cu at (100.1, 151.8)
- added C511: 1u, Resistor_SMD:R_0402_1005Metric, F.Cu at (123.8, 151.6)
- added C512: 100n, Resistor_SMD:R_0402_1005Metric, F.Cu at (123.8, 153.6)
- added C513: 100n, Resistor_SMD:R_0402_1005Metric, B.Cu at (42.4, 137.7)
- added C514: 100n, Resistor_SMD:R_0402_1005Metric, F.Cu at (100.1, 153.8)
- added C515: 1u, Resistor_SMD:R_0402_1005Metric, B.Cu at (41.3, 137.7)
- added C516: 1u, Resistor_SMD:R_0402_1005Metric, F.Cu at (100.1, 155.8)
- added C517: 330p, Resistor_SMD:R_0402_1005Metric, B.Cu at (41.8, 136.2)
- added C518: 330p, Resistor_SMD:R_0402_1005Metric, F.Cu at (100.1, 157.8)
- added C519: 100n, Resistor_SMD:R_0402_1005Metric, B.Cu at (35.0, 137.7)
- added C520: 100n, Resistor_SMD:R_0402_1005Metric, F.Cu at (123.8, 155.5)
- added C521: 1u, Resistor_SMD:R_0402_1005Metric, B.Cu at (34.0, 137.7)
- added C522: 1u, Resistor_SMD:R_0402_1005Metric, F.Cu at (123.8, 157.5)
- added C523: 100n, Resistor_SMD:R_0402_1005Metric, B.Cu at (43.3, 135.7)
- added C524: 100n, Resistor_SMD:R_0402_1005Metric, F.Cu at (103.0, 147.9)
- added C525: 330p, Resistor_SMD:R_0402_1005Metric, B.Cu at (34.5, 136.2)
- added C526: 330p, Resistor_SMD:R_0402_1005Metric, F.Cu at (126.7, 149.6)
- added C527: 330p, Resistor_SMD:R_0402_1005Metric, B.Cu at (45.4, 135.8)
- added C528: 330p, Resistor_SMD:R_0402_1005Metric, F.Cu at (103.0, 149.8)
- added C529: 100n, Resistor_SMD:R_0402_1005Metric, B.Cu at (36.0, 135.7)
- added C530: 100n, Resistor_SMD:R_0402_1005Metric, F.Cu at (126.7, 151.6)
- added C531: 330p, Resistor_SMD:R_0402_1005Metric, B.Cu at (38.1, 135.7)
- added C532: 330p, Resistor_SMD:R_0402_1005Metric, F.Cu at (126.7, 153.6)
- added C533: 100n, Resistor_SMD:R_0402_1005Metric, B.Cu at (46.5, 134.0)
- added C534: 100n, Resistor_SMD:R_0402_1005Metric, F.Cu at (103.0, 151.8)
- added C535: 1u, Resistor_SMD:R_0402_1005Metric, B.Cu at (38.8, 48.6)
- added C701: 4.7u, Resistor_SMD:R_0402_1005Metric, B.Cu at (94.7, 51.6)
- added C702: 100n, Resistor_SMD:R_0402_1005Metric, B.Cu at (104.1, 51.0)
- added C703: 100n, Resistor_SMD:R_0402_1005Metric, B.Cu at (93.6, 51.6)
- added C801: 22u, Resistor_SMD:R_0805_2012Metric, B.Cu at (49.2, 33.3)
- added C901: 1u, Resistor_SMD:R_0402_1005Metric, B.Cu at (50.0, 139.7)
- added C902: 1u, Resistor_SMD:R_0402_1005Metric, B.Cu at (84.2, 135.6)
- added C903: 100n, Resistor_SMD:R_0402_1005Metric, B.Cu at (50.0, 138.6)
- added C904: 100n, Resistor_SMD:R_0402_1005Metric, B.Cu at (84.2, 136.6)
- added C905: 1u, Resistor_SMD:R_0402_1005Metric, B.Cu at (51.3, 149.2)
- added C906: 1u, Resistor_SMD:R_0402_1005Metric, B.Cu at (49.8, 150.2)
- added C907: 1u, Resistor_SMD:R_0402_1005Metric, B.Cu at (85.4, 146.2)
- added C908: 1u, Resistor_SMD:R_0402_1005Metric, B.Cu at (83.9, 147.2)
- added C909: 100n, Resistor_SMD:R_0402_1005Metric, B.Cu at (57.7, 145.8)
- added C910: 100n, Resistor_SMD:R_0402_1005Metric, B.Cu at (57.7, 139.2)
- added C911: 100n, Resistor_SMD:R_0402_1005Metric, B.Cu at (196.1, 75.5)
- added C912: 100n, Resistor_SMD:R_0402_1005Metric, B.Cu at (205.8, 71.5)
- added C913: 100n, Resistor_SMD:R_0402_1005Metric, B.Cu at (205.9, 78.2)
- added C914: 100n, Resistor_SMD:R_0402_1005Metric, B.Cu at (197.8, 78.2)
- added D206: BLU, LED_SMD:LED_0402_1005Metric, F.Cu at (199.1, 103.3)
- added D207: GRN, LED_SMD:LED_0402_1005Metric, F.Cu at (205.3, 108.2)
- added D208: BLU, LED_SMD:LED_0402_1005Metric, F.Cu at (195.8, 103.2)
- added D209: BLU, LED_SMD:LED_0402_1005Metric, F.Cu at (202.1, 108.2)
- added D210: BLU, LED_SMD:LED_0402_1005Metric, F.Cu at (208.8, 103.5)
- added D211: BLU, LED_SMD:LED_0402_1005Metric, F.Cu at (198.4, 108.2)
- added D212: BLU, LED_SMD:LED_0402_1005Metric, F.Cu at (214.4, 103.7)
- added D213: BLU, LED_SMD:LED_0402_1005Metric, F.Cu at (195.5, 108.1)
- added D214: BLU, LED_SMD:LED_0402_1005Metric, F.Cu at (211.3, 103.5)
- added D301: 15, Diode_SMD:D_SMA, B.Cu at (225.6, 47.9)
- added D302: GRN, LED_SMD:LED_0402_1005Metric, F.Cu at (220.0, 34.8)
- added D303: GRN, LED_SMD:LED_0402_1005Metric, F.Cu at (258.1, 25.7)
- added D304: GRN, LED_SMD:LED_0402_1005Metric, F.Cu at (220.2, 43.0)
- added D305: GRN, LED_SMD:LED_0402_1005Metric, F.Cu at (258.1, 32.2)
- added D405: 5.1, Diode_SMD:D_SOD-123, F.Cu at (162.7, 158.3)
- added D502: 3.3, Diode_SMD:D_SOD-123, F.Cu at (110.3, 148.5)
- added D503: 3.3, Diode_SMD:D_SOD-123, B.Cu at (35.9, 133.5)
- added D504: 3.3, Diode_SMD:D_SOD-123, F.Cu at (134.0, 155.1)
- added D602: 150, Diode_SMD:D_SMA, F.Cu at (113.8, 82.2)
- added D603: 150, Diode_SMD:D_SMA, B.Cu at (105.6, 91.1)
- added D701: CDSOT23-T24CAN, footprints:bourns_CDSOT23_T24CAN, B.Cu at (105.2, 61.1)
- added D801: 0.5, Diode_SMD:D_SMA, B.Cu at (53.0, 31.5)
- added D901: 0.5, Diode_SMD:D_SMA, F.Cu at (51.2, 153.1)
- added D902: 0.5, Diode_SMD:D_SMA, F.Cu at (85.3, 150.0)
- added D903: BLU, LED_SMD:LED_0402_1005Metric, F.Cu at (61.0, 161.2)
- added D904: BLU, LED_SMD:LED_0402_1005Metric, F.Cu at (75.4, 156.1)
- added D905: 0.5, Diode_SMD:D_SMA, F.Cu at (60.0, 149.4)
- added D906: 0.5, Diode_SMD:D_SMA, F.Cu at (77.5, 144.6)
- added FB201: FerriteBead, Resistor_SMD:R_0402_1005Metric, B.Cu at (70.5, 51.8)
- added H801: M2.5, MountingHole:MountingHole_2.5mm, F.Cu at (157.2, 183.8)
- added H802: M2.5, MountingHole:MountingHole_2.5mm, F.Cu at (150.2, 186.8)
- added H803: M2.5, MountingHole:MountingHole_2.5mm, F.Cu at (157.2, 189.2)
- added H804: M2.5, MountingHole:MountingHole_2.5mm, F.Cu at (164.5, 189.2)
- added J202: Conn_ARM_SWD_TagConnect_TC2030-NL, Connector:Tag-Connect_TC2030-IDC-NL_2x03_P1.27mm_Vertical, F.Cu at (74.6, 27.0)
- added J203: USB_C_Plug_USB2.0, Connector_USB:USB_C_Receptacle_GCT_USB4105-xx-A_16P_TopMnt_Horizontal, F.Cu at (106.7, 26.7)
- added J501: Conn_01x03, Connector_JST:JST_PH_B3B-PH-K_1x03_P2.00mm_Vertical, F.Cu at (35.5, 46.1)
- added J502: Conn_01x03, Connector_JST:JST_PH_B3B-PH-K_1x03_P2.00mm_Vertical, F.Cu at (41.0, 55.1)
- added J503: Conn_01x03, Connector_JST:JST_PH_B3B-PH-K_1x03_P2.00mm_Vertical, F.Cu at (42.1, 42.1)
- added J504: Conn_01x03, Connector_JST:JST_PH_B3B-PH-K_1x03_P2.00mm_Vertical, F.Cu at (36.6, 51.0)
- added J701: CAN Header, footprints:molex_microfit_43650_0427, F.Cu at (123.1, 60.2)
- added J702: CAN Header, footprints:molex_microfit_43650_0427, F.Cu at (112.4, 60.2)
- added JP201: Jumper_2_Bridged, Connector_PinHeader_2.54mm:PinHeader_1x02_P2.54mm_Vertical, F.Cu at (68.3, 28.2)
- added JP202: Jumper_2_Bridged, Connector_PinHeader_2.54mm:PinHeader_1x02_P2.54mm_Vertical, F.Cu at (64.7, 28.3)
- added JP301: Jumper_2_Bridged, Connector_PinHeader_2.54mm:PinHeader_1x02_P2.54mm_Vertical, F.Cu at (229.3, 37.1)
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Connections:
- C201 pad 1: +12V -> GND
- C201 pad 2: GND -> /controller/HSE_IN
- C301 pad 1: /V_ARR+ -> GND
- C301 pad 2: GND -> Net-(D301-A2)
- C302 pad 1: /V_ARR+ -> Net-(D301-A2)
- C302 pad 2: GND -> Net-(U301-EN)
- C303 pad 1: /V_BATT+ -> +12V
- C304 pad 1: /V_BATT+ -> +5V
- C305 pad 1: /V_BATT+ -> +12V
- C401 pad 1: GND -> /gate_driver/VBUS_DRIVE_3V3
- C401 pad 2: +5V -> GND
- C402 pad 1: GND -> /gate_driver/SWH+
- C402 pad 2: +5V -> /V_{SW}
- C403 pad 1: GND -> /gate_driver/VBUS_DRIVE_5V0
- C403 pad 2: +5V -> GNDPWR
- C501 pad 1: +5V -> Net-(U501-VIN)
- C501 pad 2: GND -> GNDPWR
- C502 pad 1: +5V -> Net-(U502-VIN)
- C502 pad 2: GND -> GNDPWR
- C503 pad 1: +12V -> /sensors/VBUS_SENSE_ISO
- C503 pad 2: GND -> GNDPWR
- C504 pad 1: +12V -> /sensors/VBUS_SENSE_ISO
- C504 pad 2: GND -> GNDPWR
- C505 pad 1: Net-(D501-K) -> /sensors/VBUS_SENSE_ISO
- C505 pad 2: /V_SW -> GNDPWR
- C601 pad 1: +5V -> /V_{DCI+}
- C601 pad 2: GND -> GNDPWR
- C602 pad 1: +5V -> /V_{DCI+}
- C602 pad 2: GND -> GNDPWR
- C603 pad 1: +3V3 -> /V_{DCO+}
- C603 pad 2: GND -> GNDPWR
- C604 pad 1: +3V3 -> /V_{DCO+}
- C604 pad 2: GND -> GNDPWR
- C605 pad 1: Net-(IC601-VISOOUT) -> /V_{DCO+}
- C605 pad 2: Net-(IC601-GNDISO_1) -> GNDPWR
- D401 pad 1: /controller/ARR_I -> Net-(D401-K)
- D401 pad 2: GND -> Net-(D401-A)
- D402 pad 1: /controller/ARR_V -> Net-(D402-K)
- D402 pad 2: GND -> Net-(D402-A)
- D403 pad 1: /controller/BATT_V -> /gate_driver/SWH+
- D403 pad 2: GND -> Net-(D403-A)
- D404 pad 1: /controller/BATT_I -> /SWLO
- D404 pad 2: GND -> GNDPWR
- D501 pad 2: Net-(D501-A) -> GND
- D601 pad 1: /comm_can/CAN_H -> /V_{DCI+}
- D601 pad 2: /comm_can/CAN_L -> GNDPWR
- J201 pad 1: +12V -> VDD
- J201 pad 2: GND -> Net-(J201-Pin_2)
- J301 pad 1: /converter/V_ARR- -> Net-(D301-A2)
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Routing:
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- added copper zone on F.Cu, net Net-(J501-Pin_1)
- removed copper zone on F.Cu, net +5V
- removed copper zone on In1.Cu, net +5V
- removed copper zone on F.Cu, net /V_ARR+
- removed copper zone on In1.Cu, net /V_ARR+
- removed copper zone on B.Cu, net /V_BATT+
- removed copper zone on F.Cu, net /V_BATT+
- removed copper zone on In1.Cu, net /V_BATT+
- removed copper zone on In2.Cu, net /V_BATT+
- removed copper zone on F.Cu, net /V_SW
- removed copper zone on In1.Cu, net /V_SW
- removed copper zone on B.Cu, net /converter/V_ARR-
- removed copper zone on In2.Cu, net /converter/V_ARR-
- removed copper zone on B.Cu, net /converter/V_BATT-
- removed copper zone on In2.Cu, net /converter/V_BATT-
- removed copper zone on B.Cu, net GND
- removed copper zone on In2.Cu, net GND
- removed copper zone on F.Cu, net Net-(F301-Pad1)
- removed copper zone on In1.Cu, net Net-(F301-Pad1)
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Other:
- board size 120.1 x 60 mm -> 125 x 90 mm
- board text added: "- load switch, active load protection - Remove fuses - Remove secondary load switch driver tied to active load - consider ISO672x, ISO7710 - power from primary load switch driver or 5V ISO - general - remove extraneous test points - remove sectional led power and caps, use solder bridge at power source - power reg - shrink 12V-5V buck inductor footprint - lockout control - replace resistors for l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"
- board text added: "FAN CONTROL"
- board text added: "Target board size: 90x120mm"
- board text added: "Why are you so big"
- board text removed: "LHR Solar Sunscatter Gen 2 v0.2.0 Summer 2023 Matthew Yu"
- board text removed: "LHRS Sunscatter Gen 2 v0.2.0"
- board text removed: "Trace should not modify fill. Used to remove DRC."
